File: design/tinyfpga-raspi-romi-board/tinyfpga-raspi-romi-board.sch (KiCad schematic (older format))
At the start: 72 parts, among them J1 TINYFPGA_J1, J10 ROMI_ENC_LEFT, J11 ROMI_ENC_RIGHT, J12 QTR_LEFT, J13 QTR_RIGHT, J14 SONAR_LEFT, J15 SONAR_RIGHT, J16 PWR_SEL1, J17 PWR_SEL0, J18 RPI_EXTRA, J19 ON_OFF, J2 TINYFPGA_J2, J20 ROMI_POWER, J3 Raspberry_Pi_2_3, J4 TINYFPGA_J4, J5 TINYFPGA_J5, J6 WP_JUMP, J7 ROMI_VSW, J8 FUSE_JUMP, J9 ROMI_MOTOR_DRIVE, Q1 2N7000, Q2 2N7000, Q3 2N7000, Q4 2N7000, Q5 2N7000, Q6 2N7000, Q7 2N7000, Q8 2N7000, SW2 SW_Push, SW3 SW_Push, SW4 SW_Push, U1 CAT24C128

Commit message: happy with mechanicals. routing and pin swapping
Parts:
- added H1, H2, H3, H4: MountingHole, MountingHole:MountingHole_2.5mm, symbol Mechanical:MountingHole
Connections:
- net FPGA_HBA_INT: now reaches J1.4 (Pin_4)
- net FPGA_HBA_INT: now also J3.33 (PWM1/GPIO13)
- net FPGA_BTN_RST renamed RPI_BTN0
- net RPI_BTN0: now also J3.7 (GCLK0/GPIO4)
- net RPI_GPIO13: no longer names the net of J18.5 (Pin_5)
- net RPI_GPIO13: no longer J3.33 (PWM1/GPIO13)
- net RPI_GPIO4: no longer names the net of J18.4 (Pin_4)
- net RPI_GPIO4: no longer J3.7 (GCLK0/GPIO4)
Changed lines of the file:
@@
 L power:+3.3V #PWR047
 U 1 1 5D5CDBF2
-P 8650 -1300
-F 0 "#PWR047" H 8650 -1450 50  0001 C CNN
-F 1 "+3.3V" H 8665 -1127 50  0000 C CNN
-F 2 "" H 8650 -1300 50  0001 C CNN
-F 3 "" H 8650 -1300 50  0001 C CNN
-	1    8650 -1300
+P 8550 -1300
+F 0 "#PWR047" H 8550 -1450 50  0001 C CNN
+F 1 "+3.3V" H 8565 -1127 50  0000 C CNN
+F 2 "" H 8550 -1300 50  0001 C CNN
+F 3 "" H 8550 -1300 50  0001 C CNN
+	1    8550 -1300
 	1    0    0    -1
 $EndComp
 Text Label 9750 -1100 2    50   ~ 0
-FPGA_BTN_RST
-Wire Wire Line
-	8650 -1300 8750 -1300
+RPI_BTN0
+Wire Wire Line
+	8550 -1300 8750 -1300
 Wire Wire Line
 	9050 -1300 9150 -1300
@@
 Text Notes 3600 -3850 0    50   ~ 0
 User LEDs
-Text Label 7950 5400 0    50   ~ 0
-FPGA_BTN_RST
+Text Label 9150 5200 0    50   ~ 0
+FPGA_HBA_INT
 Text Label 10850 5000 2    50   ~ 0
 FPGA_BTN0
@@
 	9100 -2450 8600 -2450
 Wire Wire Line
-	12350 -1850 11850 -1850
-Wire Wire Line
-	12350 -1750 11850 -1750
+	12450 -1850 11850 -1850
+Wire Wire Line
+	12450 -1750 11850 -1750
 Wire Wire Line
 	12350 -2450 11850 -2450
@@
 Wire Wire Line
 	12350 -3150 11850 -3150
-Text Label 12350 -1750 2    50   ~ 0
-RPI_GPIO13
-Text Label 12350 -1850 2    50   ~ 0
+Text Label 12450 -1850 2    50   ~ 0
 RPI_GPIO12
 Text Label 12350 -2450 2    50   ~ 0
@@
 Text Label 12350 -3150 2    50   ~ 0
 RPI_GPIO2
-Text Label 12350 -2850 2    50   ~ 0
-RPI_GPIO4
 Wire Wire Line
 	9100 -2950 8600 -2950
 Wire Wire Line
-	9100 -3050 8600 -3050
-Wire Wire Line
 	9100 -3250 8600 -3250
 Wire Wire Line
-	9100 -3150 8600 -3150
-Wire Wire Line
 	9100 -3450 8600 -3450
 Wire Wire Line
 	9100 -3350 8600 -3350
-Text Label 9100 -3050 2    50   ~ 0
-RPI_GPIO13
 Text Label 9100 -2950 2    50   ~ 0
 RPI_GPIO12
@@
 Text Label 9100 -3350 2    50   ~ 0
 RPI_GPIO2
-Text Label 9100 -3150 2    50   ~ 0
-RPI_GPIO4
 Wire Notes Line
 	4150 1150 1550 1150
@@
 	-1   0    0    -1
 $EndComp
+Text Label 12350 -2850 2    50   ~ 0
+RPI_BTN0
+Text Label 12450 -1750 2    50   ~ 0
+FPGA_HBA_INT
+$Comp
+L Mechanical:MountingHole H2
+U 1 1 5D205B99
+P 1850 6700
+F 0 "H2" H 1950 6746 50  0000 L CNN
+F 1 "MountingHole" H 1950 6655 50  0000 L CNN
+F 2 "MountingHole:MountingHole_2.5mm" H 1850 6700 50  0001 C CNN
+F 3 "~" H 1850 6700 50  0001 C CNN
+	1    1850 6700
+	1    0    0    -1
+$EndComp
+$Comp
+L Mechanical:MountingHole H3
+U 1 1 5D206F31
+P 1800 7050
+F 0 "H3" H 1900 7096 50  0000 L CNN
+F 1 "MountingHole" H 1900 7005 50  0000 L CNN
+F 2 "MountingHole:MountingHole_2.5mm" H 1800 7050 50  0001 C CNN
+F 3 "~" H 1800 7050 50  0001 C CNN
+	1    1800 7050
+	1    0    0    -1
+$EndComp
+$Comp
+L Mechanical:MountingHole H4
+U 1 1 5D23E212
+P 1800 7300
+F 0 "H4" H 1900 7346 50  0000 L CNN
+F 1 "MountingHole" H 1900 7255 50  0000 L CNN
+F 2 "MountingHole:MountingHole_2.5mm" H 1800 7300 50  0001 C CNN
+F 3 "~" H 1800 7300 50  0001 C CNN
+	1    1800 7300
+	1    0    0    -1
+$EndComp
+$Comp
+L Mechanical:MountingHole H1
+U 1 1 5D23E5EE
+P 1900 6300
+F 0 "H1" H 2000 6346 50  0000 L CNN
+F 1 "MountingHole" H 2000 6255 50  0000 L CNN
+F 2 "MountingHole:MountingHole_2.5mm" H 1900 6300 50  0001 C CNN
+F 3 "~" H 1900 6300 50  0001 C CNN
+	1    1900 6300
+	1    0    0    -1
+$EndComp
 $EndSCHEMATC

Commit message: mostly done routing but have a few more rpi signals to deal with
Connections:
- net FPGA_BTN0: now also J4.8 (Pin_8); no longer J2.2 (Pin_2)
- net FPGA_BTN1: now also J1.12 (Pin_12); no longer J2.3 (Pin_3)
- net FPGA_HBA_INT: now also J2.12 (Pin_12); no longer J1.4 (Pin_4)
- net FPGA_LED0: now also J1.10 (Pin_10); no longer J2.14 (Pin_14)
- net FPGA_LED1: now also J4.6 (Pin_6); no longer J4.1 (Pin_1)
- net FPGA_LED2: now also J1.7 (Pin_7); no longer J4.5 (Pin_5)
- net FPGA_LED3: now also J4.5 (Pin_5); no longer J4.7 (Pin_7)
- net FPGA_LED4: now also J1.9 (Pin_9); no longer J4.2 (Pin_2)
- net FPGA_LED5: now also J1.8 (Pin_8); no longer J4.6 (Pin_6)
- net FPGA_LED6: now also J4.1 (Pin_1); no longer J4.8 (Pin_8)
- net FPGA_LED7: now also J1.6 (Pin_6); no longer J5.2 (Pin_2)
- net QTRL_CTRL: now also J5.2 (Pin_2); no longer J1.13 (Pin_13)
- net QTRL_OUT: now also J1.4 (Pin_4); no longer J1.14 (Pin_14)
- net QTRR_CTRL: now also J1.14 (Pin_14); no longer J1.11 (Pin_11)
- net QTRR_OUT: now also J1.13 (Pin_13); no longer J1.12 (Pin_12)
- net ROMI_DIRL: now also J2.5 (Pin_5); no longer J2.7 (Pin_7)
- net ROMI_DIRR: now also J2.8 (Pin_8); no longer J2.10 (Pin_10)
- net ROMI_ENC_LA: now also J2.3 (Pin_3); no longer J2.5 (Pin_5)
- net ROMI_ENC_LB: now also J2.2 (Pin_2); no longer J2.4 (Pin_4)
- net ROMI_ENC_RA: now also J2.14 (Pin_14); no longer J2.13 (Pin_13)
- net ROMI_ENC_RB: now also J2.13 (Pin_13); no longer J2.12 (Pin_12)
- net ROMI_PWML: now also J2.6 (Pin_6); no longer J2.8 (Pin_8)
- net ROMI_PWMR: now also J2.9 (Pin_9); no longer J2.11 (Pin_11)
- net ROMI_~SLPL: now also J2.4 (Pin_4); no longer J2.6 (Pin_6)
- net ROMI_~SLPR: now also J2.7 (Pin_7); no longer J2.9 (Pin_9)
- net RPI_RXD: now also J2.11 (Pin_11); no longer J1.6 (Pin_6)
- net RPI_TXD: now also J2.10 (Pin_10); no longer J1.5 (Pin_5)
- net SONL_ECHO: now also J1.5 (Pin_5); no longer J1.8 (Pin_8)
- net SONL_TRIG: now also J4.2 (Pin_2); no longer J1.7 (Pin_7)
- net SONR_ECHO: now also J1.11 (Pin_11); no longer J1.10 (Pin_10)
- net SONR_TRIG: now also J4.7 (Pin_7); no longer J1.9 (Pin_9)
- net VREG_OUT: now reaches A1.4 (+VOUT), F1.2, J8.2 (Pin_2)
- net VRP: now reaches J7.11 (Pin_11), J7.7 (Pin_7), J7.9 (Pin_9)
- net VB: now reaches J7.13 (Pin_13), J7.15 (Pin_15)
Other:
- note removed: "TODO:\n* Add Mill-Max 0906-1-15-20-75-14-11-0 to break out WP. What's pin 10 for?\n* Change header genders to be consistent (male up / female down)\n* Change jumper to full size not half size"
- moved on the sheet: F1, H1, H2, H3, H4, J12, J13, J14, J15, J8, R10, R23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

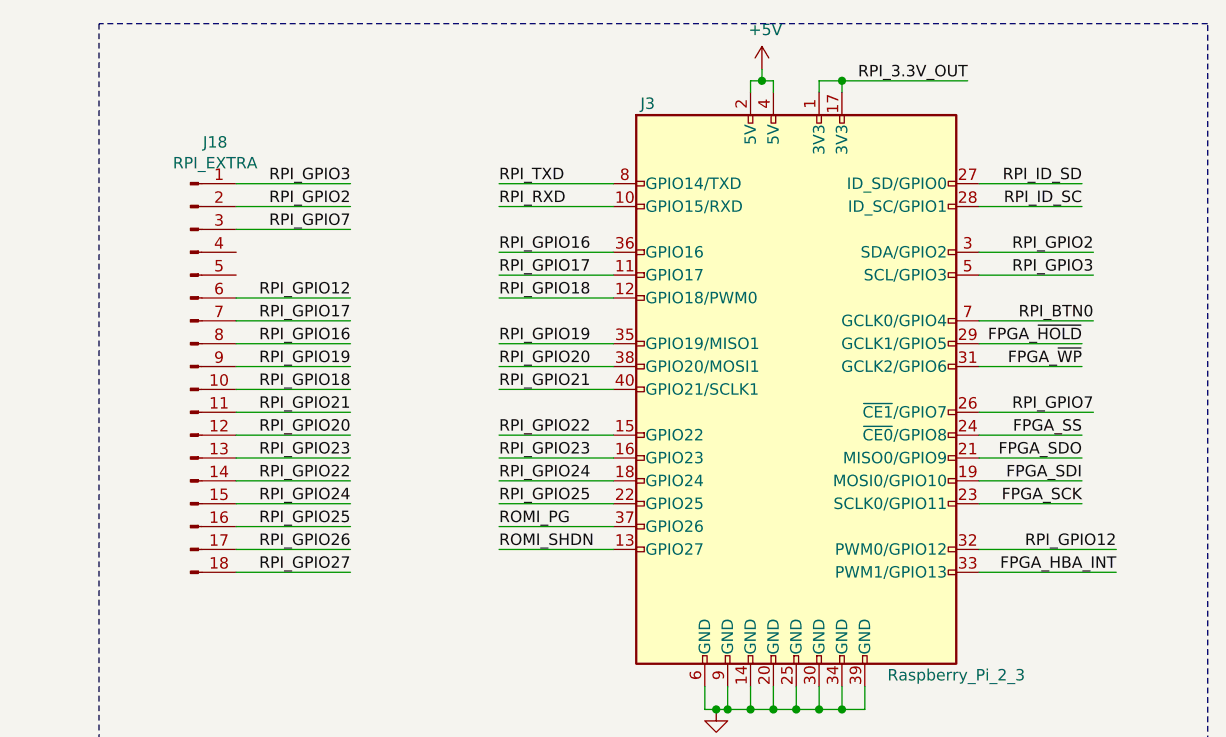
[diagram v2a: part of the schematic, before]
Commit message: signals routed. needs silk and drc
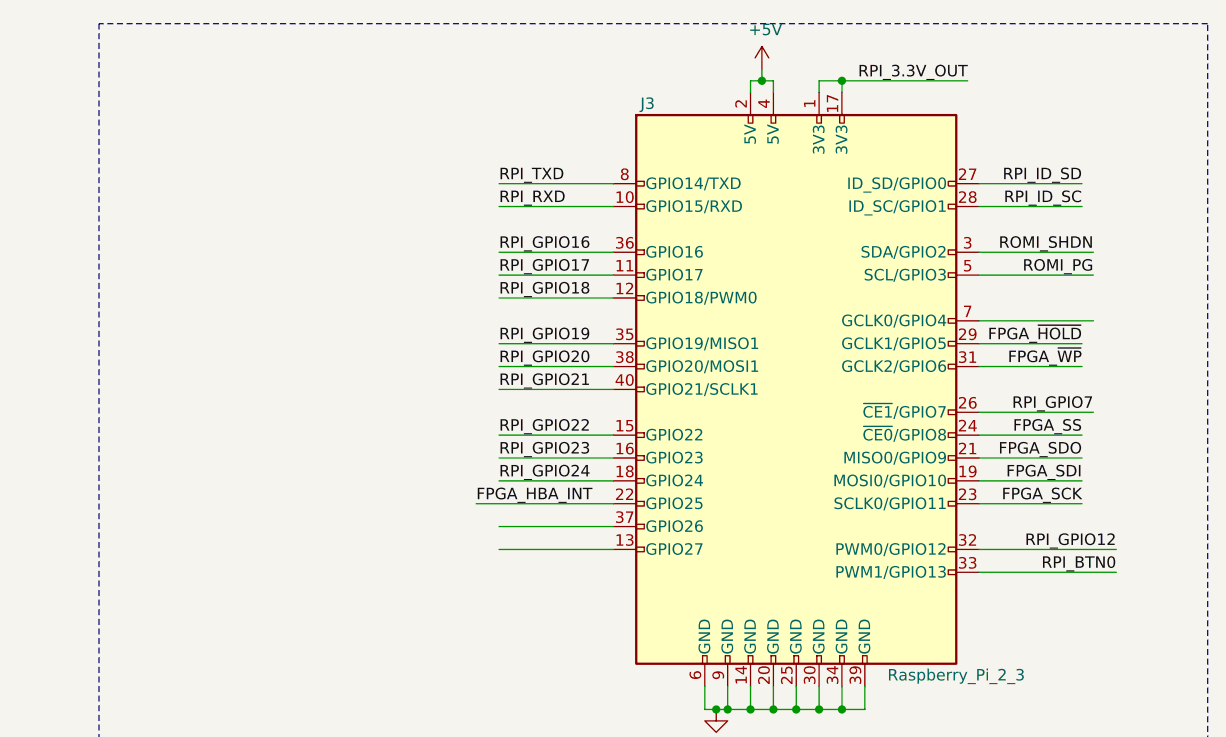
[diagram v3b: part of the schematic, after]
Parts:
- removed J18: RPI_EXTRA, Connector_PinHeader_2.54mm:PinHeader_1x18_P2.54mm_Vertical, symbol Connector:Conn_01x18_Male
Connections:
- net RPI_GPIO2 is gone; now on net ROMI_SHDN: J3.3 (SDA/GPIO2)
- net RPI_GPIO25 is gone; now on net FPGA_HBA_INT: J3.22 (GPIO25)
- net RPI_GPIO3 is gone; now on net ROMI_PG: J3.5 (SCL/GPIO3)
- net FPGA_HBA_INT: no longer J3.33 (PWM1/GPIO13)
- net ROMI_PG: no longer J3.37 (GPIO26)
- net ROMI_SHDN: no longer J3.13 (GPIO27)
- net RPI_BTN0: now also J3.33 (PWM1/GPIO13); no longer J3.7 (GCLK0/GPIO4)
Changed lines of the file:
@@
 Text Label 9750 -2150 0    50   ~ 0
 RPI_GPIO24
-Text Label 9750 -2050 0    50   ~ 0
-RPI_GPIO25
-Text Label 9750 -1950 0    50   ~ 0
+Text Label 12350 -3050 2    50   ~ 0
 ROMI_PG
-Text Label 9750 -1850 0    50   ~ 0
+Text Label 12350 -3150 2    50   ~ 0
 ROMI_SHDN
 Wire Wire Line
@@
 	9750 -2150 10250 -2150
 Wire Wire Line
-	10250 -2050 9750 -2050
+	10250 -2050 9650 -2050
 Wire Wire Line
 	9750 -1950 10250 -1950
@@
 Wire Wire Line
 	9750 -2550 10250 -2550
-Text Label 9100 -2150 2    50   ~ 0
-RPI_GPIO22
-Text Label 9100 -2250 2    50   ~ 0
-RPI_GPIO23
-Text Label 9100 -1950 2    50   ~ 0
-RPI_GPIO25
-Text Label 9100 -1750 2    50   ~ 0
-RPI_GPIO27
-Wire Wire Line
-	9100 -2150 8600 -2150
-Wire Wire Line
-	8600 -2250 9100 -2250
-Wire Wire Line
-	8600 -1950 9100 -1950
-Wire Wire Line
-	8600 -1750 9100 -1750
-Text Label 9100 -2450 2    50   ~ 0
-RPI_GPIO21
-Text Label 9100 -2350 2    50   ~ 0
-RPI_GPIO20
-Text Label 9100 -2650 2    50   ~ 0
-RPI_GPIO19
-Text Label 9100 -2550 2    50   ~ 0
-RPI_GPIO18
-Text Label 9100 -2850 2    50   ~ 0
-RPI_GPIO17
-Text Label 9100 -2750 2    50   ~ 0
-RPI_GPIO16
-Wire Wire Line
-	9100 -2750 8600 -2750
-Wire Wire Line
-	9100 -2850 8600 -2850
-Wire Wire Line
-	9100 -2550 8600 -2550
-Wire Wire Line
-	9100 -2650 8600 -2650
-Wire Wire Line
-	9100 -2350 8600 -2350
-Wire Wire Line
-	9100 -2450 8600 -2450
 Wire Wire Line
 	12450 -1850 11850 -1850
@@
 Text Label 12350 -2450 2    50   ~ 0
 RPI_GPIO7
-Text Label 12350 -3050 2    50   ~ 0
-RPI_GPIO3
-Text Label 12350 -3150 2    50   ~ 0
-RPI_GPIO2
-Wire Wire Line
-	9100 -2950 8600 -2950
-Wire Wire Line
-	9100 -3250 8600 -3250
-Wire Wire Line
-	9100 -3450 8600 -3450
-Wire Wire Line
-	9100 -3350 8600 -3350
-Text Label 9100 -2950 2    50   ~ 0
-RPI_GPIO12
-Text Label 9100 -3250 2    50   ~ 0
-RPI_GPIO7
-Text Label 9100 -3450 2    50   ~ 0
-RPI_GPIO3
-Text Label 9100 -3350 2    50   ~ 0
-RPI_GPIO2
 Wire Notes Line
 	4150 1150 1550 1150
@@
 	-1   0    0    -1
 $EndComp
-$Comp
-L Connector:Conn_01x18_Male J18
-U 1 1 5D0E8841
-P 8400 -2650
-F 0 "J18" H 8508 -1669 50  0000 C CNN
-F 1 "RPI_EXTRA" H 8508 -1760 50  0000 C CNN
-F 2 "Connector_PinHeader_2.54mm:PinHeader_1x18_P2.54mm_Vertical" H 8400 -2650 50  0001 C CNN
-F 3 "~" H 8400 -2650 50  0001 C CNN
-	1    8400 -2650
-	1    0    0    -1
-$EndComp
-Text Label 9100 -1850 2    50   ~ 0
-RPI_GPIO26
-Text Label 9100 -2050 2    50   ~ 0
-RPI_GPIO24
-Wire Wire Line
-	8600 -1850 9100 -1850
-Wire Wire Line
-	9100 -2050 8600 -2050
 Text Label -3650 3500 0    50   ~ 0
 ROMI_SHDN
@@
 	-1   0    0    -1
 $EndComp
-Text Label 12350 -2850 2    50   ~ 0
+Text Label 12450 -1750 2    50   ~ 0
 RPI_BTN0
-Text Label 12450 -1750 2    50   ~ 0
+Text Label 9650 -2050 0    50   ~ 0
 FPGA_HBA_INT
 $Comp

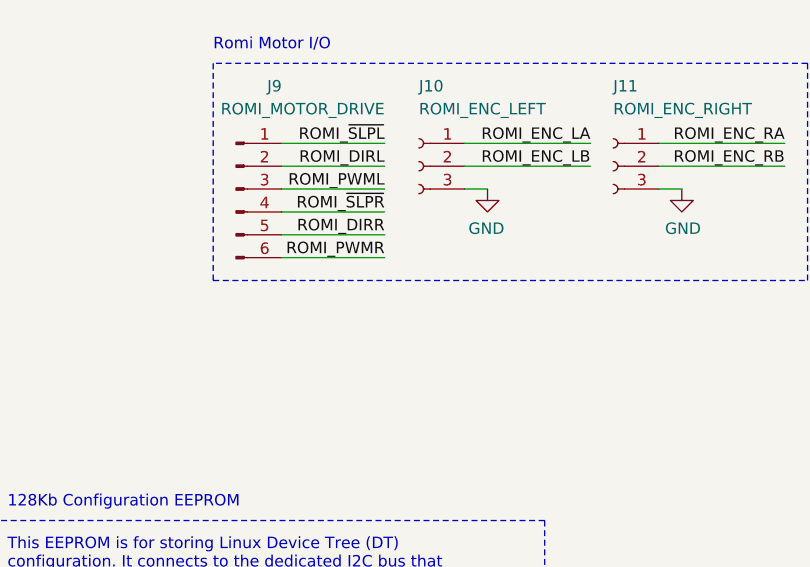
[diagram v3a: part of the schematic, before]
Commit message: changed mount hole size and aligned them better. added pwm pulldowns
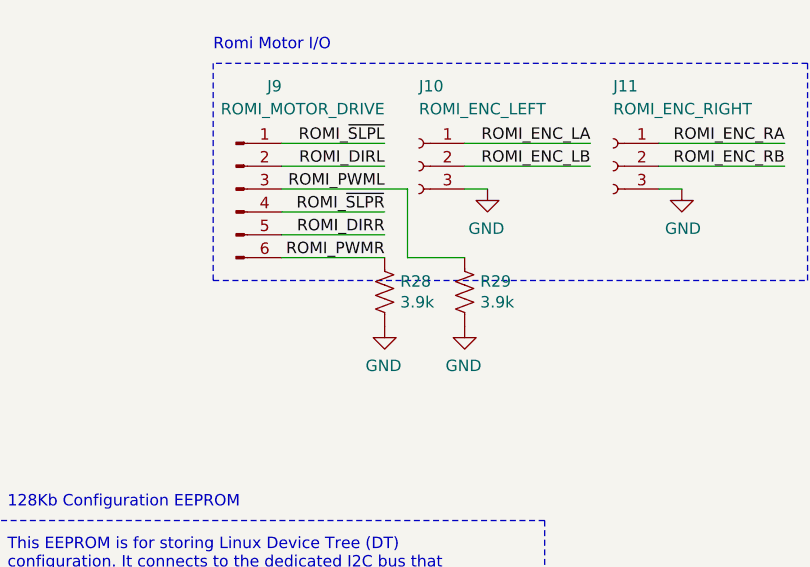
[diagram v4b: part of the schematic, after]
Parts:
- added R28, R29: 3.9k, Resistor_THT:R_Axial_DIN0204_L3.6mm_D1.6mm_P2.54mm_Vertical, symbol Device:R_US
- H1, H2, H3, H4: footprint MountingHole:MountingHole_2.5mm -> MountingHole:MountingHole_2.7mm_M2.5
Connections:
- net GND: now also R28.1, R29.1
- net ROMI_PWML: now also R29.2
- net ROMI_PWMR: now also R28.2
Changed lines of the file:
@@
 	2300 1800 1850 1800
-Wire Wire Line
-	1850 1700 2300 1700
 Wire Wire Line
 	2300 1600 1850 1600
@@
 F 0 "H2" H 700 7296 50  0000 L CNN
 F 1 "MountingHole" H 700 7205 50  0000 L CNN
-F 2 "MountingHole:MountingHole_2.5mm" H 600 7250 50  0001 C CNN
+F 2 "MountingHole:MountingHole_2.7mm_M2.5" H 600 7250 50  0001 C CNN
 F 3 "~" H 600 7250 50  0001 C CNN
 	1    600  7250
@@
 F 0 "H3" H 700 7496 50  0000 L CNN
 F 1 "MountingHole" H 700 7405 50  0000 L CNN
-F 2 "MountingHole:MountingHole_2.5mm" H 600 7450 50  0001 C CNN
+F 2 "MountingHole:MountingHole_2.7mm_M2.5" H 600 7450 50  0001 C CNN
 F 3 "~" H 600 7450 50  0001 C CNN
 	1    600  7450
@@
 F 0 "H4" H 700 7696 50  0000 L CNN
 F 1 "MountingHole" H 700 7605 50  0000 L CNN
-F 2 "MountingHole:MountingHole_2.5mm" H 600 7650 50  0001 C CNN
+F 2 "MountingHole:MountingHole_2.7mm_M2.5" H 600 7650 50  0001 C CNN
 F 3 "~" H 600 7650 50  0001 C CNN
 	1    600  7650
@@
 F 0 "H1" H 700 7096 50  0000 L CNN
 F 1 "MountingHole" H 700 7005 50  0000 L CNN
-F 2 "MountingHole:MountingHole_2.5mm" H 600 7050 50  0001 C CNN
+F 2 "MountingHole:MountingHole_2.7mm_M2.5" H 600 7050 50  0001 C CNN
 F 3 "~" H 600 7050 50  0001 C CNN
 	1    600  7050
@@
 Wire Wire Line
 	-1150 1550 -1050 1550
+$Comp
+L Device:R_US R28
+U 1 1 5D146B5E
+P 2300 2150
+F 0 "R28" H 2232 2104 50  0000 R CNN
+F 1 "3.9k" H 2232 2195 50  0000 R CNN
+F 2 "Resistor_THT:R_Axial_DIN0204_L3.6mm_D1.6mm_P2.54mm_Vertical" V 2340 2140 50  0001 C CNN
+F 3 "~" H 2300 2150 50  0001 C CNN
+	1    2300 2150
+	-1   0    0    1
+$EndComp
+$Comp
+L Device:R_US R29
+U 1 1 5D147C58
+P 2650 2150
+F 0 "R29" H 2582 2104 50  0000 R CNN
+F 1 "3.9k" H 2582 2195 50  0000 R CNN
+F 2 "Resistor_THT:R_Axial_DIN0204_L3.6mm_D1.6mm_P2.54mm_Vertical" V 2690 2140 50  0001 C CNN
+F 3 "~" H 2650 2150 50  0001 C CNN
+	1    2650 2150
+	-1   0    0    1
+$EndComp
+Wire Wire Line
+	2400 1700 2400 2000
+Wire Wire Line
+	2400 2000 2650 2000
+Wire Wire Line
+	1850 1700 2400 1700
+$Comp
+L power:GND #PWR0104
+U 1 1 5D17CC58
+P 2300 2300
+F 0 "#PWR0104" H 2300 2050 50  0001 C CNN
+F 1 "GND" H 2305 2127 50  0000 C CNN
+F 2 "" H 2300 2300 50  0001 C CNN
+F 3 "" H 2300 2300 50  0001 C CNN
+	1    2300 2300
+	-1   0    0    -1
+$EndComp
+$Comp
+L power:GND #PWR0105
+U 1 1 5D17D014
+P 2650 2300
+F 0 "#PWR0105" H 2650 2050 50  0001 C CNN
+F 1 "GND" H 2655 2127 50  0000 C CNN
+F 2 "" H 2650 2300 50  0001 C CNN
+F 3 "" H 2650 2300 50  0001 C CNN
+	1    2650 2300
+	-1   0    0    -1
+$EndComp
 $EndSCHEMATC
